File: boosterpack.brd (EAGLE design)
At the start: 76.5 x 55.9 mm, 27 parts, among them J1 POWERPOLE_DOUBLE

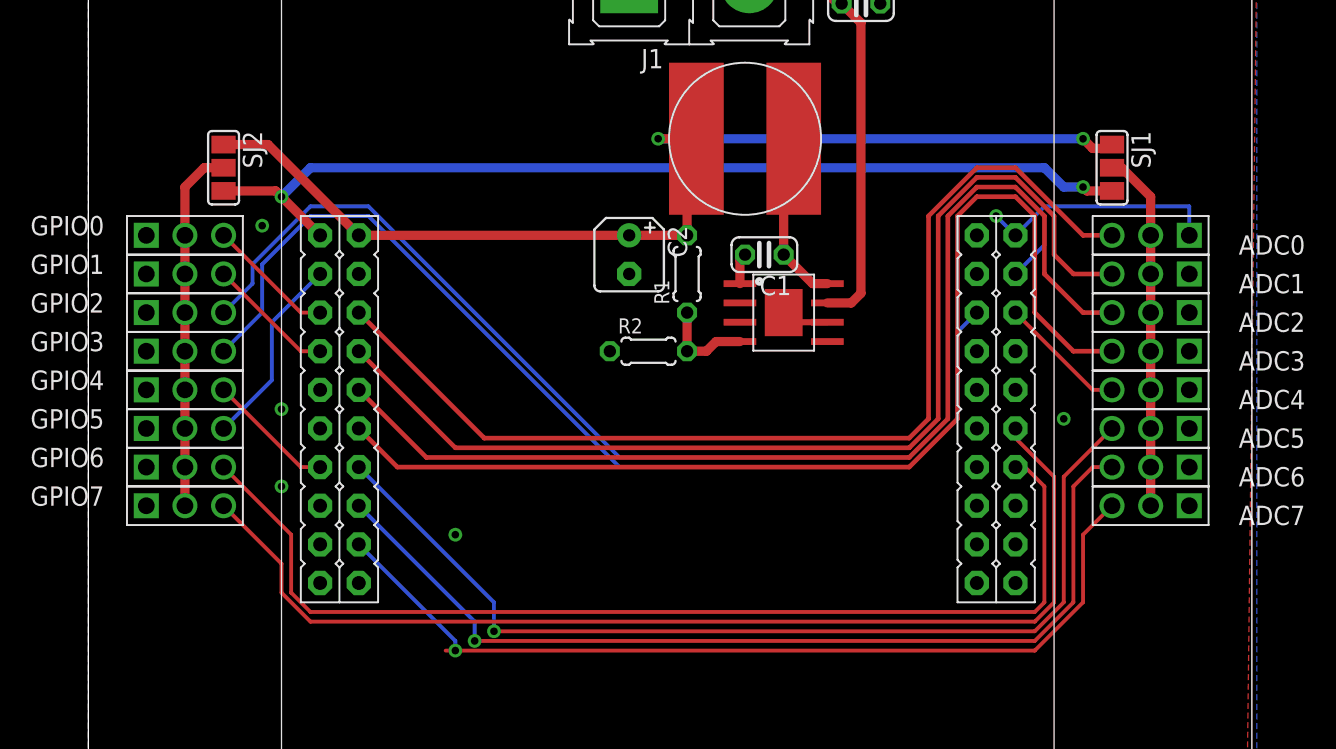
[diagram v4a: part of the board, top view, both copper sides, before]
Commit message: flipped the adc's and the gpio's; fewer wires are going across the middle
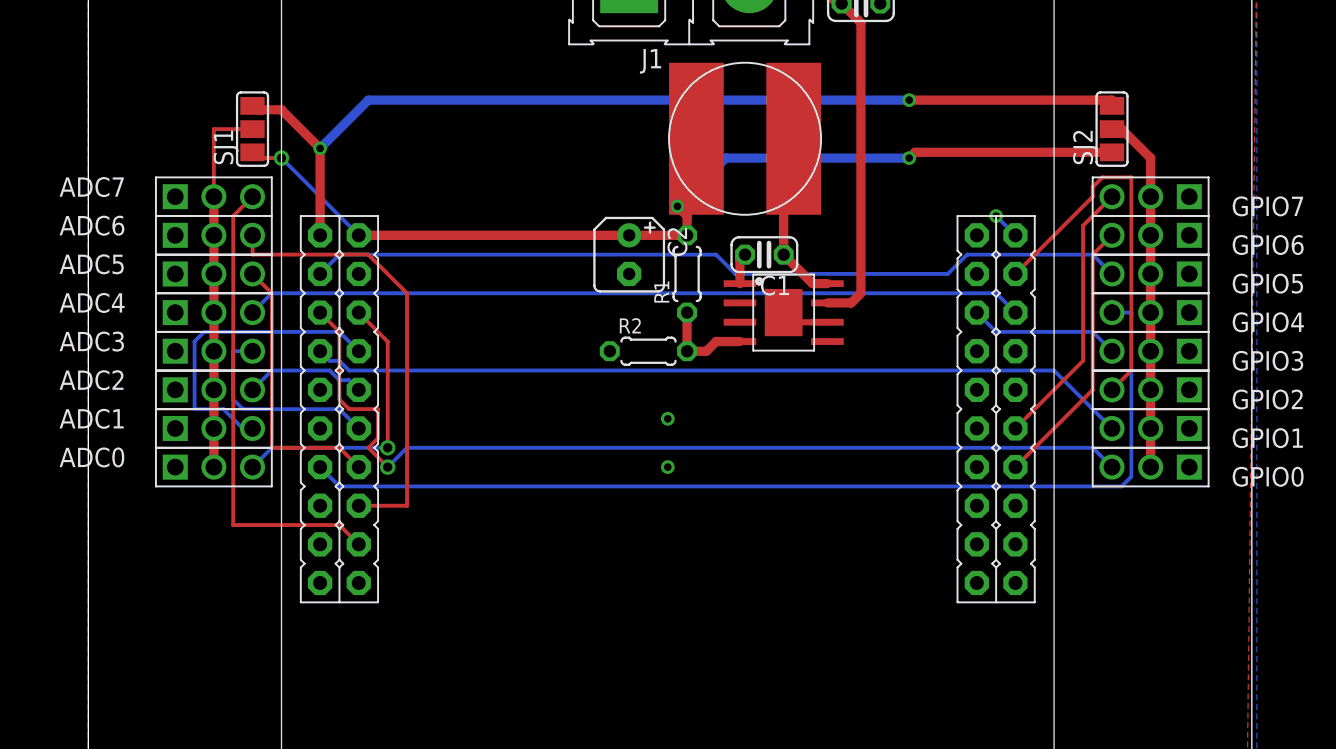
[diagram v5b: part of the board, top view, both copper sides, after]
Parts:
- moved GPIO7 71.5 mm to (82.5, 63.5), turned to 180 degrees
- moved GPIO0 70.3 mm to (82.5, 45.7), turned to 180 degrees
- moved GPIO6 70.3 mm to (82.5, 61.0), turned to 180 degrees
- moved ADC7 69.7 mm to (15.9, 63.5), turned to 0 degrees
- moved GPIO1 69.3 mm to (82.5, 48.3), turned to 180 degrees
- moved GPIO5 69.3 mm to (82.5, 58.4), turned to 180 degrees
- moved GPIO2 68.8 mm to (82.5, 50.8), turned to 180 degrees
- moved GPIO4 68.8 mm to (82.5, 55.9), turned to 180 degrees
- moved GPIO3 68.6 mm to (82.5, 53.3), turned to 180 degrees
- moved ADC0 68.4 mm to (15.9, 45.7), turned to 0 degrees
- moved ADC6 68.4 mm to (15.9, 61.0), turned to 0 degrees
- moved ADC1 67.4 mm to (15.9, 48.3), turned to 0 degrees
- moved ADC5 67.4 mm to (15.9, 58.4), turned to 0 degrees
- moved ADC2 66.9 mm to (15.9, 50.8), turned to 0 degrees
- moved ADC4 66.9 mm to (15.9, 55.9), turned to 0 degrees
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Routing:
- net ADC2: track 72.2 -> 8.04 mm
- net ADC3: track 73.7 -> 13.5 mm
- net GPIO2: track 85.0 -> 25.1 mm
- net GPIO3: track 69.5 -> 9.94 mm
- net N$2: track 8.45 -> 66.2 mm
- net N$8: track 71.9 -> 17.9 mm
- net GPIO0: track 8.45 -> 62.3 mm, vias 0 -> 1
- net N$6: track 70.5 -> 17.9 mm
- net ADC1: track 71.5 -> 20.4 mm
- net N$1: track 70.0 -> 19.1 mm, vias 0 -> 1
- net ADC5: track 65.5 -> 18.2 mm, vias 1 -> 0
- net GPIO1: track 8.45 -> 54.2 mm
- net N$13: track 8.45 -> 51.2 mm
- net N$3: track 12.8 -> 54.2 mm
- net N$4: track 63.2 -> 29.6 mm, vias 1 -> 0
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
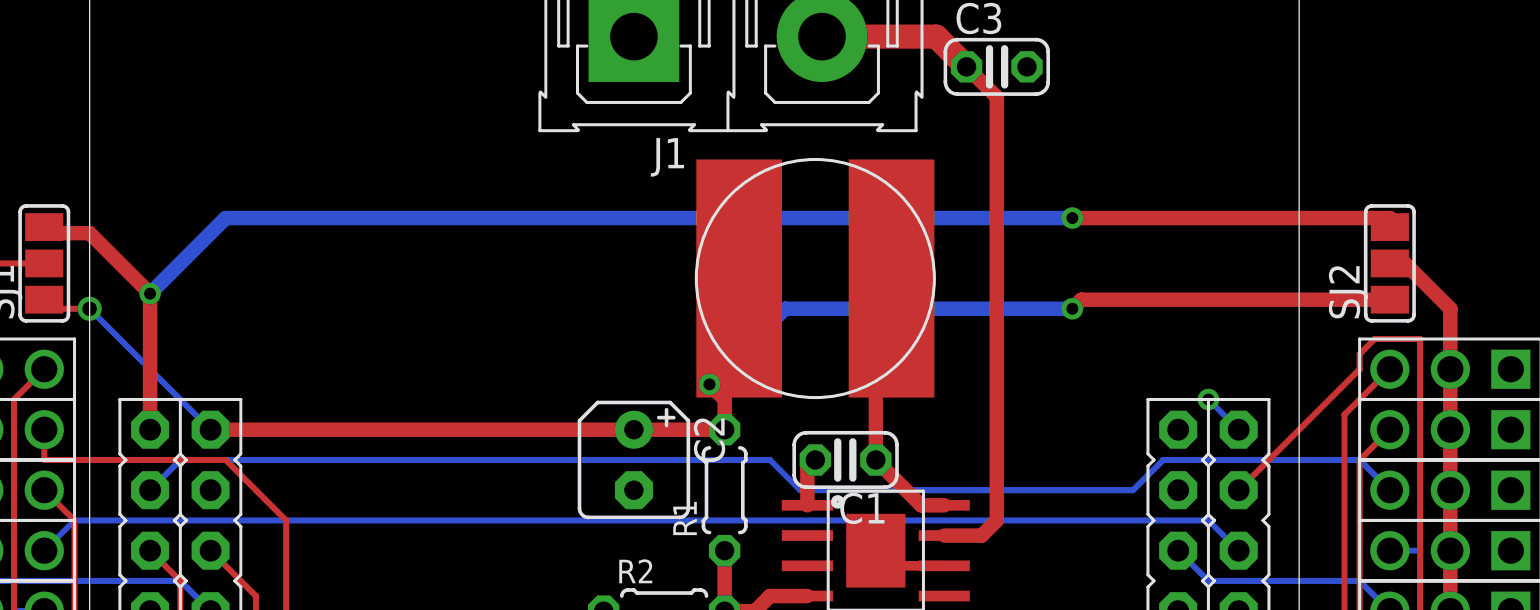
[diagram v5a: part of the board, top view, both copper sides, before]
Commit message: added diode i forgot; routed new diode
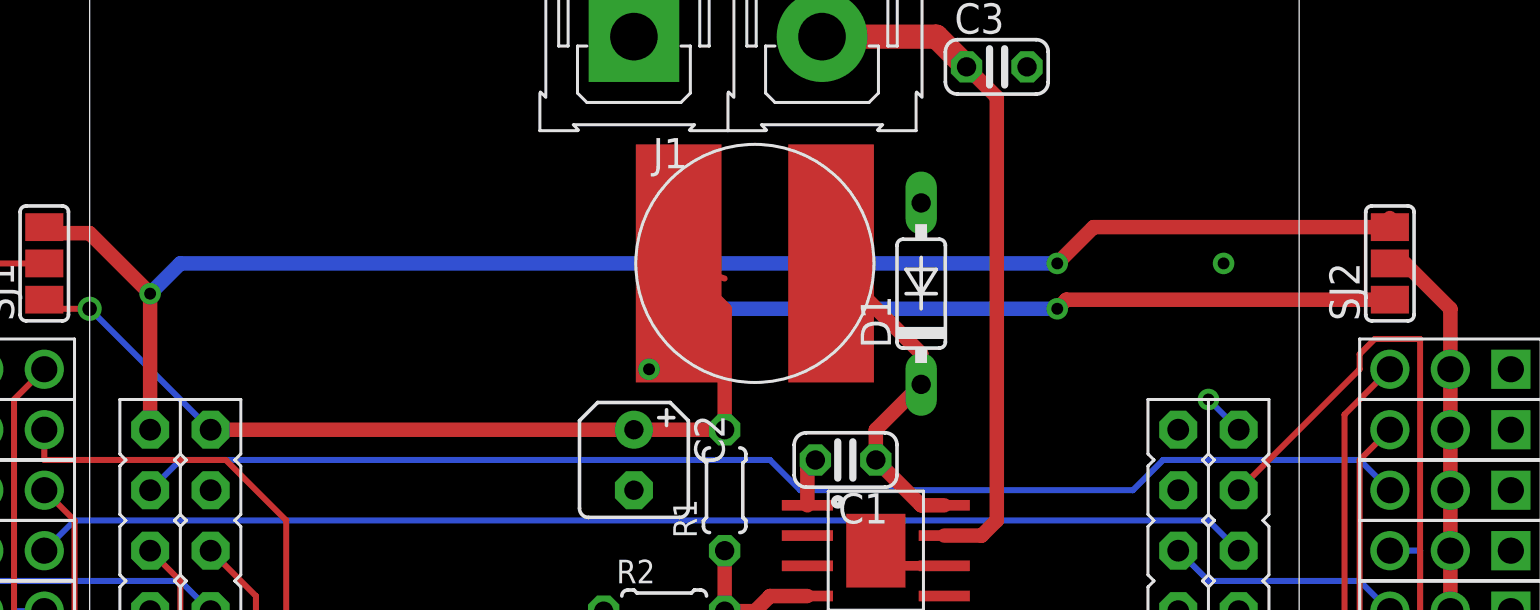
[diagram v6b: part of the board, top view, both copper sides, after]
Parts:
- added D1: (no value), diode:DO35-7
- moved L1 2.62 mm to (50.8, 67.9)
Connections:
- net GND: now also D1.A
- net N$11: now also D1.C
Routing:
- net +5V: track 70.2 -> 73.2 mm, vias 3 -> 2
- net N$11: track 11.6 -> 14.3 mm
- net GND: vias 3 -> 4
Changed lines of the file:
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@@
 <element name="U$2" library="packages(ti)" package="DDS" value="TPS5450" x="55.88" y="55.88"/>
 <element name="C1" library="resistor" package="C025-024X044" value="10nF" x="54.61" y="59.69" rot="R180"/>
-<element name="L1" library="RASEagleLib" package="SDR1006" value="10uH" x="53.34" y="67.31" rot="R270"/>
+<element name="L1" library="RASEagleLib" package="SDR1006" value="10uH" x="50.8" y="67.945" rot="R270"/>
 <element name="R1" library="resistor" package="0204/5" value="10k" x="49.53" y="58.42" rot="R90"/>
 <element name="R2" library="resistor" package="0204/5" value="3.24k" x="46.99" y="53.34"/>
@@
 <element name="SJ1" library="jumper" package="SJ_2" value="" x="20.955" y="67.945" rot="R90"/>
 <element name="SJ2" library="jumper" package="SJ_2" value="" x="77.47" y="67.945" rot="R90"/>
+<element name="D1" library="diode" package="DO35-7" value="" x="57.785" y="66.675" rot="R90"/>
 </elements>
 <signals>
@@
 <wire x1="27.94" y1="60.96" x2="22.86" y2="66.04" width="0.254" layer="16"/>
 <wire x1="20.955" y1="66.04" x2="20.955" y2="66.421" width="0.254" layer="1"/>
-<wire x1="49.53" y1="60.96" x2="49.53" y2="67.31" width="0.254" layer="1"/>
-<wire x1="49.53" y1="67.31" x2="50.14" y2="67.31" width="0.254" layer="1"/>
+<wire x1="49.53" y1="67.31" x2="47.6" y2="67.945" width="0.254" layer="1"/>
 <via x="22.86" y="66.04" extent="1-16" drill="0.6096"/>
 <wire x1="49.53" y1="60.96" x2="45.72" y2="60.96" width="0.6096" layer="1"/>
 <wire x1="27.94" y1="60.96" x2="45.72" y2="60.96" width="0.6096" layer="1"/>
-<wire x1="77.47" y1="66.421" x2="64.516" y2="66.421" width="0.6096" layer="1"/>
-<wire x1="64.516" y1="66.421" x2="64.135" y2="66.04" width="0.6096" layer="1"/>
-<via x="64.135" y="66.04" extent="1-16" drill="0.5"/>
-<wire x1="64.135" y1="66.04" x2="52.07" y2="66.04" width="0.6096" layer="16"/>
-<wire x1="52.07" y1="66.04" x2="48.895" y2="62.865" width="0.6096" layer="16"/>
-<wire x1="49.53" y1="60.96" x2="49.53" y2="62.23" width="0.6096" layer="1"/>
-<wire x1="49.53" y1="62.23" x2="48.895" y2="62.865" width="0.6096" layer="1"/>
-<via x="48.895" y="62.865" extent="1-16" drill="0.5"/>
+<wire x1="49.53" y1="60.96" x2="49.53" y2="66.015" width="0.6096" layer="1"/>
+<wire x1="49.53" y1="66.015" x2="47.6" y2="67.945" width="0.6096" layer="1"/>
+<wire x1="77.47" y1="66.421" x2="63.881" y2="66.421" width="0.6096" layer="1"/>
+<wire x1="63.881" y1="66.421" x2="63.5" y2="66.04" width="0.6096" layer="1"/>
+<via x="63.5" y="66.04" extent="1-16" drill="0.5"/>
+<wire x1="63.5" y1="66.04" x2="48.895" y2="66.04" width="0.6096" layer="16"/>
+<wire x1="48.895" y1="66.04" x2="46.355" y2="63.5" width="0.6096" layer="16"/>
+<wire x1="49.53" y1="66.015" x2="48.895" y2="66.04" width="0" layer="19" extent="1-16"/>
 </signal>
 <signal name="GND">
@@
 <via x="48.26" y="48.895" extent="1-16" drill="0.5"/>
 <via x="48.26" y="45.72" extent="1-16" drill="0.5"/>
+<contactref element="D1" pad="A"/>
+<via x="70.485" y="67.945" extent="1-16" drill="0.5"/>
 </signal>
 <signal name="N$10">
@@
 <wire x1="58.755" y1="57.785" x2="57.785" y2="57.785" width="0.6096" layer="1"/>
 <wire x1="57.785" y1="57.785" x2="55.88" y2="59.69" width="0.6096" layer="1"/>
-<wire x1="55.88" y1="59.69" x2="55.88" y2="64.77" width="0.6096" layer="1"/>
-<wire x1="55.88" y1="64.77" x2="56.515" y2="65.405" width="0.6096" layer="1"/>
-<wire x1="56.515" y1="65.405" x2="56.515" y2="67.285" width="0.6096" layer="1"/>
-<wire x1="56.515" y1="67.285" x2="56.54" y2="67.31" width="0.6096" layer="1"/>
+<contactref element="D1" pad="C"/>
+<wire x1="55.88" y1="59.69" x2="55.88" y2="60.96" width="0.6096" layer="1"/>
+<wire x1="55.88" y1="60.96" x2="57.785" y2="62.865" width="0.6096" layer="1"/>
+<wire x1="57.785" y1="62.865" x2="57.785" y2="64.16" width="0.6096" layer="1"/>
+<wire x1="57.785" y1="64.16" x2="54" y2="67.945" width="0.6096" layer="1"/>
 </signal>
 <signal name="VCC">
@@
 <via x="25.4" y="66.675" extent="1-16" drill="0.5"/>
 <wire x1="77.47" y1="69.469" x2="77.47" y2="69.85" width="0.6096" layer="1"/>
-<wire x1="77.47" y1="69.85" x2="64.135" y2="69.85" width="0.6096" layer="1"/>
-<via x="64.135" y="69.85" extent="1-16" drill="0.5"/>
-<wire x1="64.135" y1="69.85" x2="28.575" y2="69.85" width="0.6096" layer="16"/>
-<wire x1="28.575" y1="69.85" x2="25.4" y2="66.675" width="0.6096" layer="16"/>
+<wire x1="77.47" y1="69.469" x2="65.024" y2="69.469" width="0.6096" layer="1"/>
+<wire x1="65.024" y1="69.469" x2="63.5" y2="67.945" width="0.6096" layer="1"/>
+<via x="63.5" y="67.945" extent="1-16" drill="0.5"/>
+<wire x1="63.5" y1="67.945" x2="26.67" y2="67.945" width="0.6096" layer="16"/>
+<wire x1="26.67" y1="67.945" x2="25.4" y2="66.675" width="0.6096" layer="16"/>
+</signal>
+<signal name="N$12">
+<via x="46.355" y="63.5" extent="1-16" drill="0.5"/>
 </signal>
 </signals>

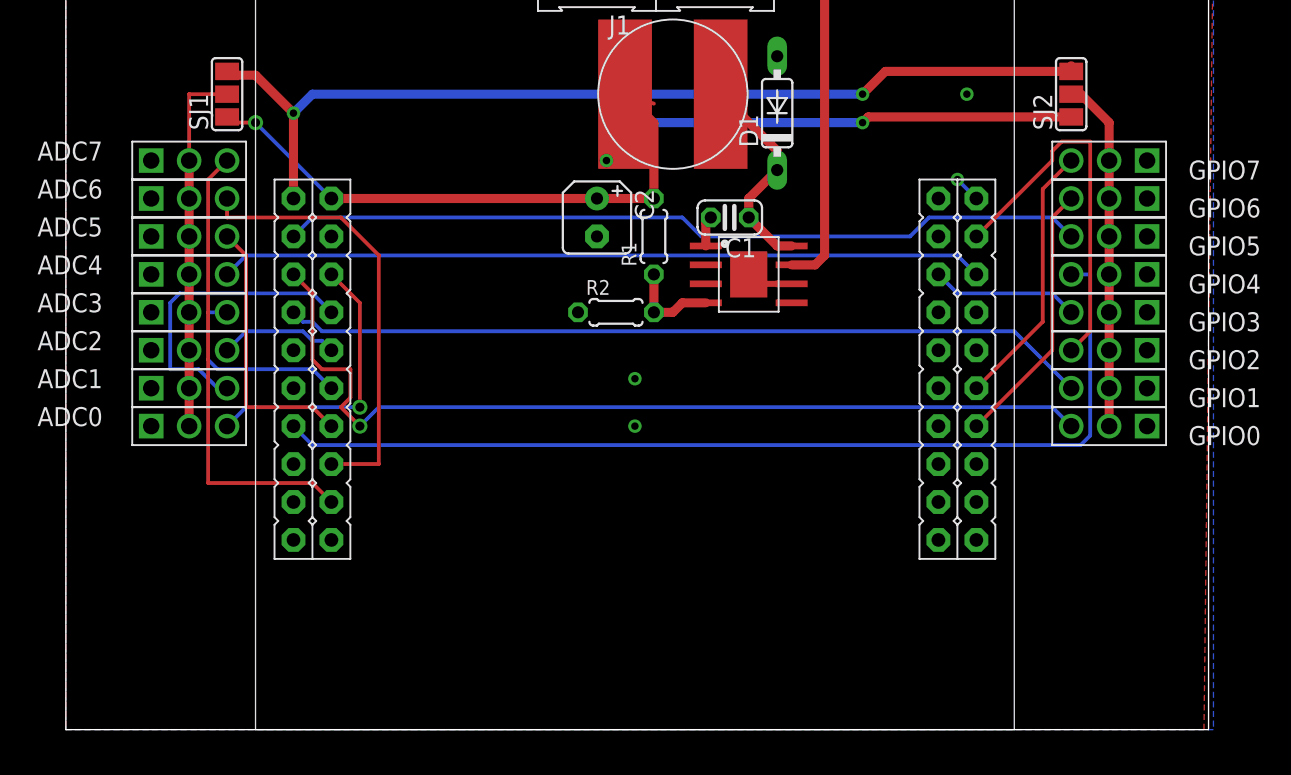
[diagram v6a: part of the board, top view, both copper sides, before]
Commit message: added spi motor driver for two motors
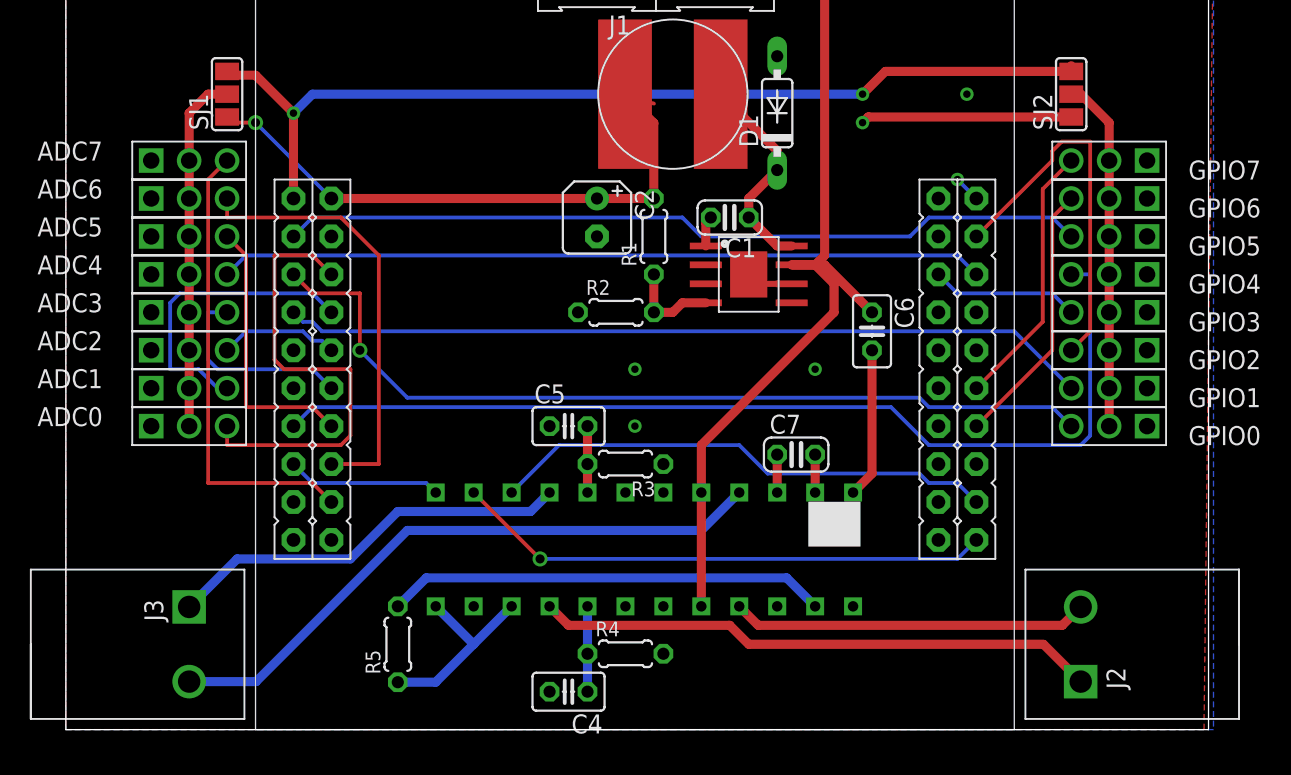
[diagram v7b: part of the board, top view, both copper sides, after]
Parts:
- added C4, C5: 0.1uF, resistor:C025-025X050
- added C6: (no value), resistor:C025-025X050
- added C7: 0.22uF, resistor:C025-024X044
- added J2, J3: PHOENIXSCREWTERMINAL_2, RASEagleLib:PHOENIXSCREWTERMINAL_2
- added R3, R4: (no value), resistor:0204/5
- added R5: 5k, resistor:0204/5
- added U$3: A3992A, RASEagleLib:DIP24
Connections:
- new net +3V3: R5.1, U$3.13, U$3.15
- new net CP2: C7.1, U$3.3
- new net MOTORCLK: U$1.PA2, U$3.11
- new net MOTORFSS: U$1.PA3, U$3.10
- new net MOTORMOSI: U$1.PA5, U$3.12
- new net N$14: J3.2, U$3.4
- new net N$15: J3.1, U$3.9
- new net N$17: J2.1, U$3.16
- new net N$18: J2.2, U$3.21
- new net N$19: C5.2, R3.2, U$3.8
- new net N$20: C4.1, R4.1, U$3.17
- new net N$21: C6.2, U$3.1
- new net N$22: R5.2, U$3.23
- new net N$23: C7.2, U$3.2
- net GND: now also C4.2, C5.1, R3.1, R4.2, U$3.18, U$3.19, U$3.6, U$3.7
- net VCC: now also C6.1, U$3.20, U$3.5
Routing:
- net N$14: track 0.00 -> 42.1 mm
- net N$17: track 0.00 -> 37.6 mm
- net MOTORCLK: track 0.00 -> 36.0 mm, vias 0 -> 1
- net MOTORFSS: track 0.00 -> 34.0 mm
- net VCC: track 28.6 -> 62.4 mm
- net N$22: track 0.00 -> 29.5 mm
- net N$15: track 0.00 -> 27.3 mm
- net N$18: track 0.00 -> 23.9 mm
- net +5V: track 73.2 -> 55.6 mm
- net +3V3: track 0.00 -> 13.3 mm
- net N$1: track 19.1 -> 30.9 mm, vias 1 -> 0
- net MOTORMOSI: track 0.00 -> 10.3 mm
- net N$21: track 0.00 -> 10.1 mm
- net N$20: track 0.00 -> 5.71 mm
- net N$19: track 0.00 -> 4.45 mm
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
